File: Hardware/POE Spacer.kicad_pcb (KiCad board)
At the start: 2 copper layers, 34 x 34 mm, 12 parts, among them J3 Conn_01x02_Male, J4 Conn_01x02_Male, J5 Conn_01x02_Male, J6 Conn_01x02_Male, J7 Conn_01x08_Male, J9 QWIIC_Stackable

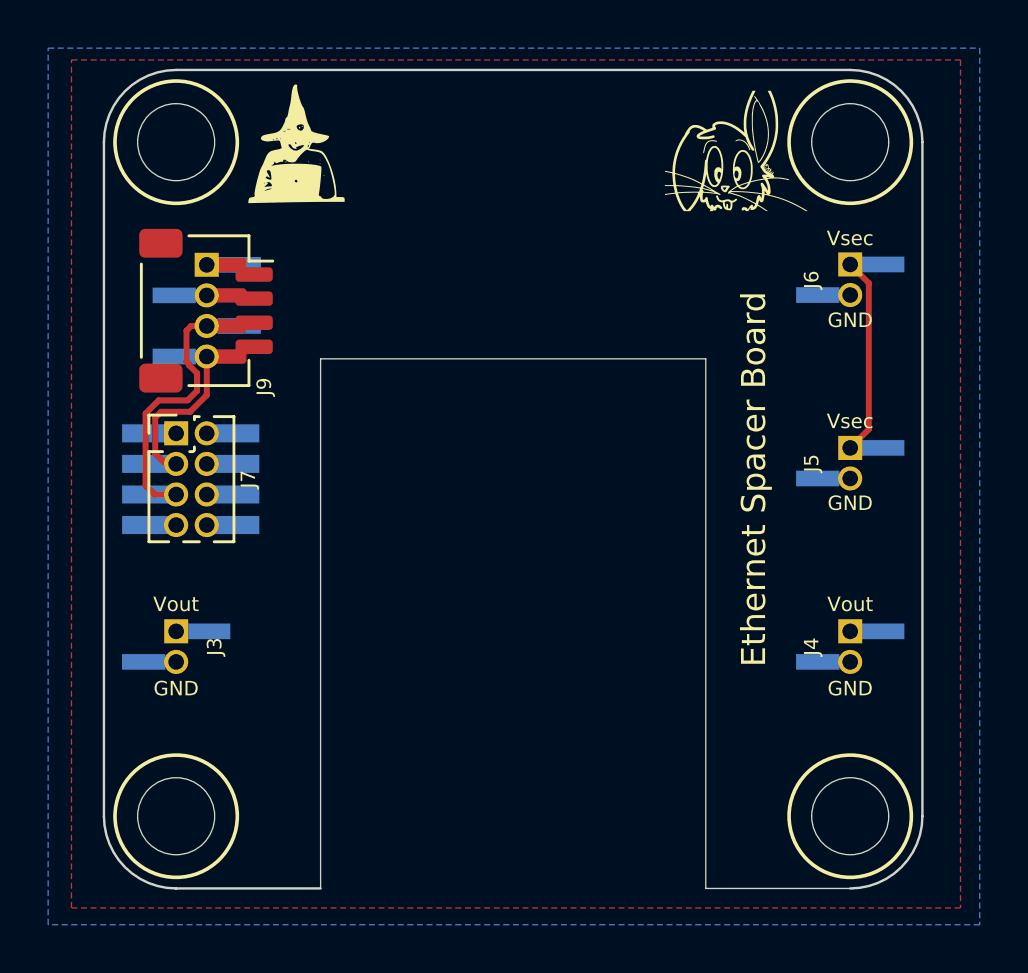
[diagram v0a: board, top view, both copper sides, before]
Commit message: Still working on changes to J7/J9...
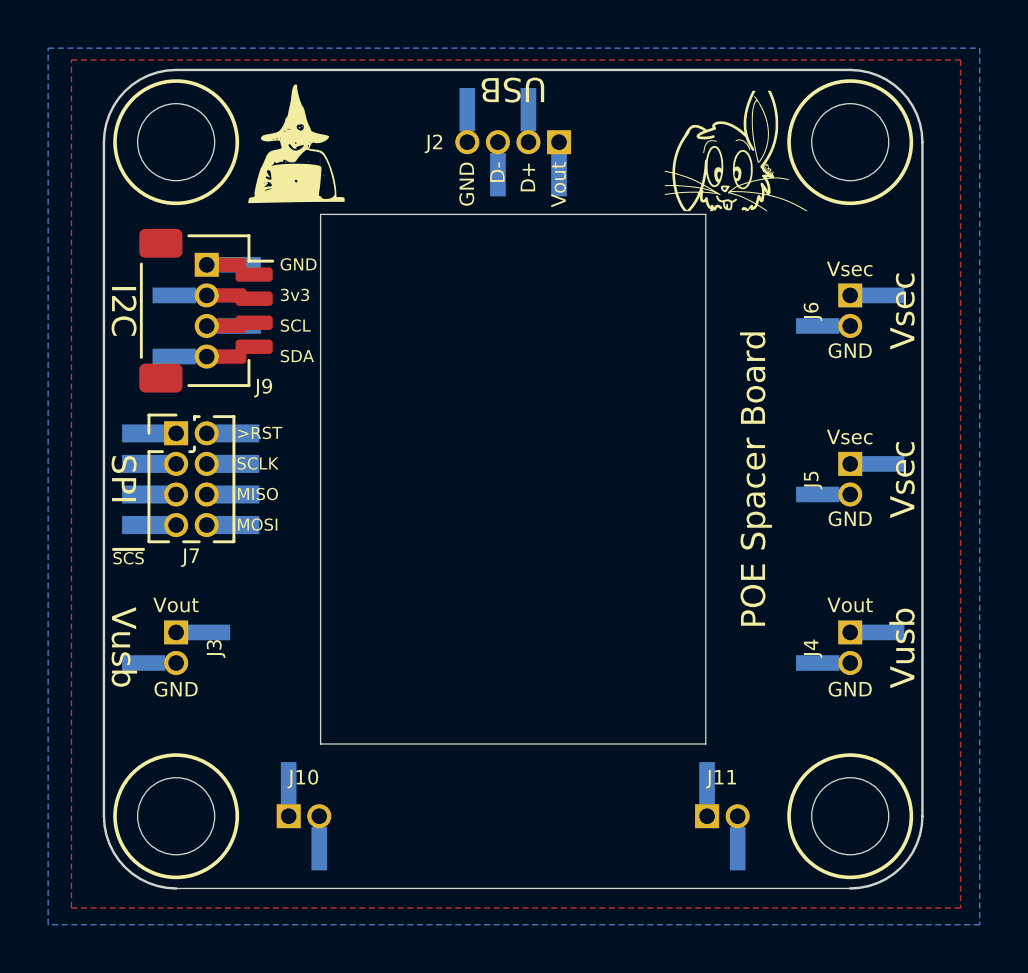
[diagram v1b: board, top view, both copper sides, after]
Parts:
- added J10: Conn_01x02_Male, Tinker:Board_Stacker_2, F.Cu at (90.7, 114.0)
- added J11: Conn_01x02_Male, Tinker:Board_Stacker_2, F.Cu at (108.1, 114.0)
- added J2: Conn_01x04_Male, Tinker:Board_Stacker_4, F.Cu at (101.9, 86.0)
- moved J6 1.28 mm to (114.0, 92.4)
- moved J5 0.66 mm to (114.0, 99.4)
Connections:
- net WIZ_RST renamed ~{SCS}3
- J5 pad 1: Vsec -> unconnected-(J5-Pad1)
- J6 pad 1: Vsec -> unconnected-(J6-Pad1)
- J7 pad 2: SCLK -> RESET
- J7 pad 3: SCL -> ~{SCS}2
- J7 pad 4: MISO -> SCLK
- J7 pad 5: SDA -> ~{SCS}1
- J7 pad 6: MOSI -> MISO
- J7 pad 7: unconnected-(J7-Pad7) -> ~{SCS}0
- J7 pad 8: ~{SCS} -> MOSI
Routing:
- net SDA: track 10.6 -> 0.00 mm
- net Vsec: track 8.26 -> 0.00 mm
- net SCL: track 6.15 -> 0.00 mm
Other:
- outline, holes or cut-outs redrawn
- board text added: "3v3"
- board text added: ">RST"
- board text added: "D+"
- board text added: "D-"
- board text added: "MISO"
- board text added: "MOSI"
- board text added: "SCL"
- board text added: "SCLK"
- board text added: "SDA"
- board text added: "SPI"
- board text added: "USB"
- board text added: "Vusb"
- board text added: "~{SCS}"

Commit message: Still migrating to 0.2.x
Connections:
- net ~{SCS}3 renamed ~{RESET}
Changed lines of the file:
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@@
   (net 8 "MISO")
   (net 9 "MOSI")
-  (net 10 "~{SCS}3")
+  (net 10 "~{RESET}")
   (net 11 "RESET")
   (net 12 "Vcc?")
@@
     (fp_line (start -1.07 4.445) (end -1.07 0.2175) (layer "F.Fab") (width 0.1))
     (pad "1" smd rect (at -1.195 0) (size 2.1 0.75) (layers "B.Cu" "B.Paste" "B.Mask")
-      (net 10 "~{SCS}3") (pinfunction "Pin_1") (pintype "passive"))
+      (net 10 "~{RESET}") (pinfunction "Pin_1") (pintype "passive"))
     (pad "1" thru_hole rect (at 0 0) (size 1 1) (drill 0.65) (layers *.Cu *.Mask)
-      (net 10 "~{SCS}3") (pinfunction "Pin_1") (pintype "passive"))
+      (net 10 "~{RESET}") (pinfunction "Pin_1") (pintype "passive"))
     (pad "2" smd rect (at 2.405 0) (size 2.1 0.75) (layers "B.Cu" "B.Paste" "B.Mask")
       (net 11 "RESET") (pinfunction "Pin_2") (pintype "passive"))
